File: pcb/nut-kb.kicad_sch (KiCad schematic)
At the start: 24 parts, among them SW1 SW_Push, U1 ATmega32U4-A, Y1 16 MHz

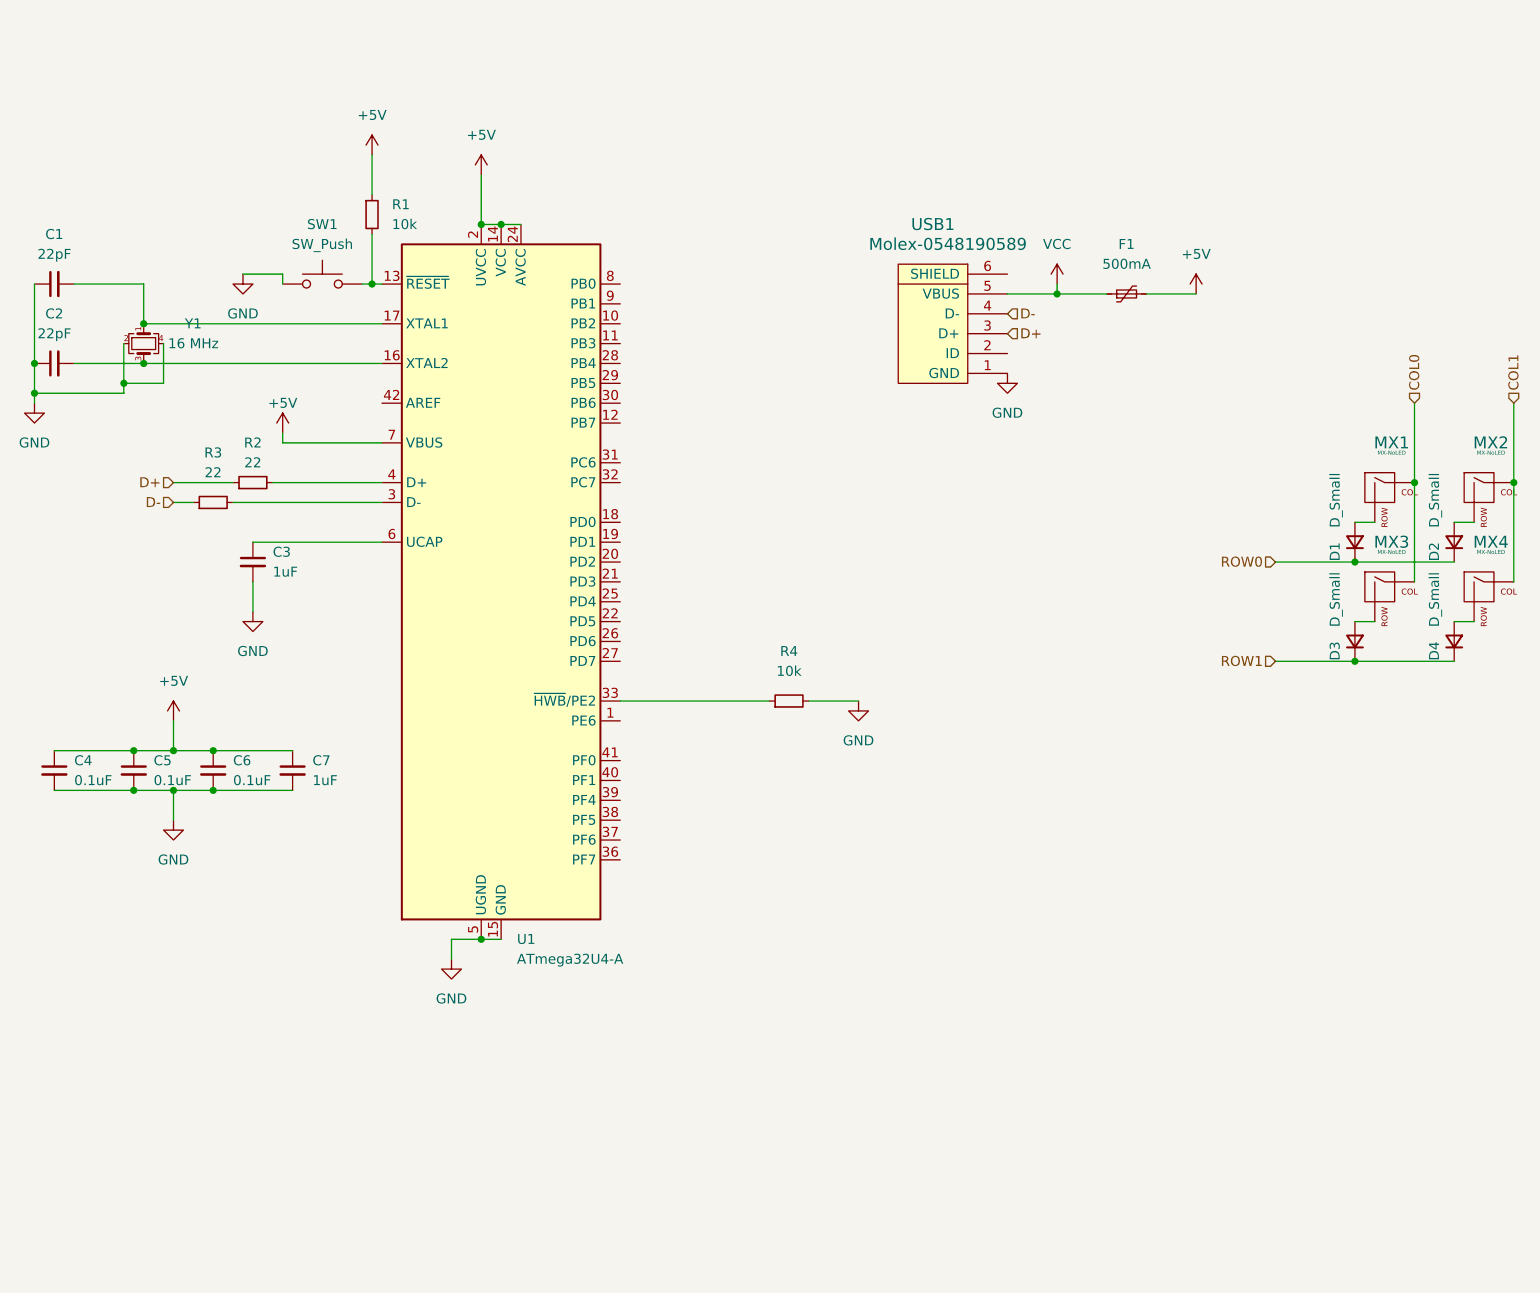
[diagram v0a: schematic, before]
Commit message: [pcb] finish everything for MX
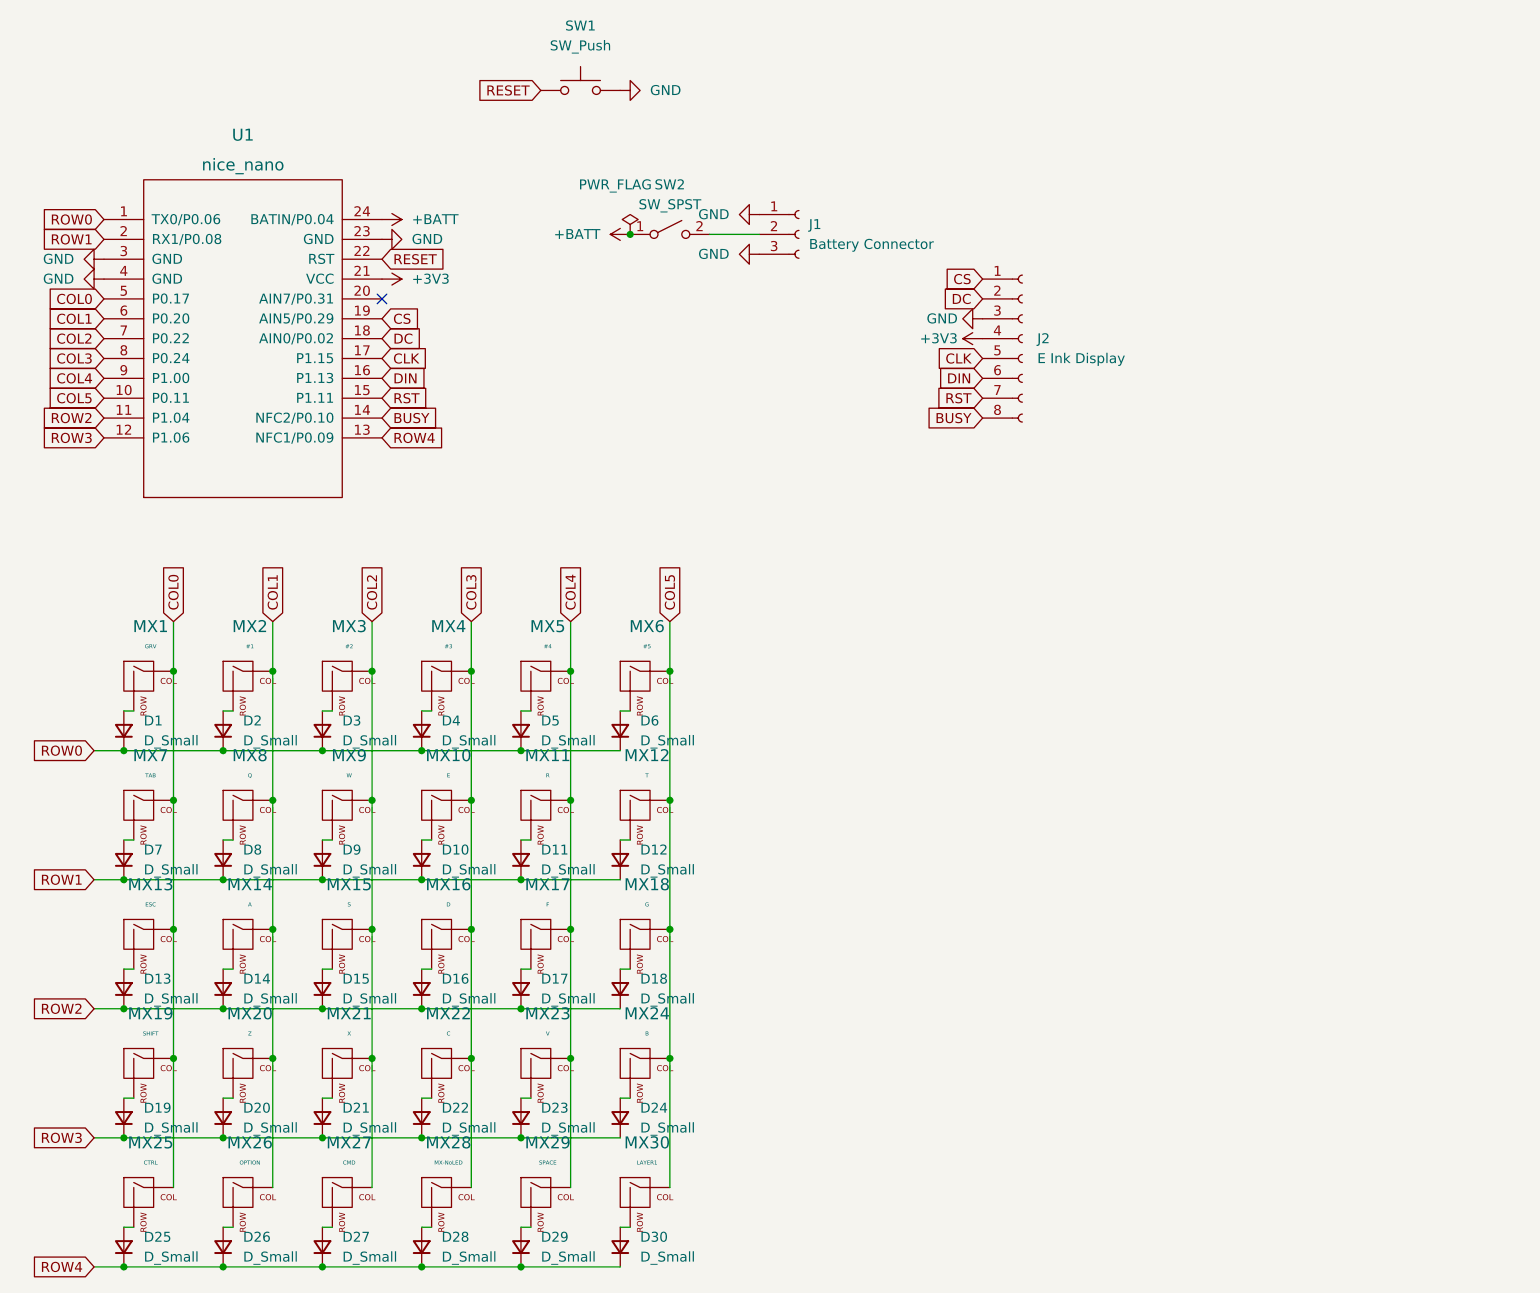
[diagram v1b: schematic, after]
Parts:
- removed C1, C2: 22pF, Capacitor_SMD:C_0805_2012Metric, symbol Device:C_Small
- removed C3, C7: 1uF, Capacitor_SMD:C_0805_2012Metric, symbol Device:C_Small
- removed C4, C5, C6: 0.1uF, Capacitor_SMD:C_0805_2012Metric, symbol Device:C_Small
- removed F1: 500mA, Fuse:Fuse_1206_3216Metric, symbol Device:Polyfuse_Small
- removed R1, R4: 10k, Resistor_SMD:R_0805_2012Metric, symbol Device:R_Small
- removed R2, R3: 22, Resistor_SMD:R_0805_2012Metric, symbol Device:R_Small
- removed U1: ATmega32U4-A, Package_QFP:TQFP-44_10x10mm_P0.8mm, symbol MCU_Microchip_ATmega:ATmega32U4-A
- removed USB1: Molex-0548190589, random-keyboard-parts:Molex-0548190589, symbol random-keyboard-parts:Molex-0548190589
- removed Y1: 16 MHz, Package_QFP:TQFP-44_10x10mm_P0.8mm, symbol Device:Crystal_GND24_Small
- added D10, D11, D12, D13, D14, D15, D16, D17, D18, D19, D20, D21, D22, D23, D24, D25, D26, D27, D28, D29, D30, D5, D6, D7, D8, D9: D_Small, Diode_SMD:D_SOD-123, symbol Device:D_Small
- added J1: Battery Connector, Connector_JST:JST_PH_B3B-PH-K_1x03_P2.00mm_Vertical, symbol Connector:Conn_01x03_Female
- added J2: E Ink Display, Connector_PinSocket_2.54mm:PinSocket_1x08_P2.54mm_Vertical, symbol Connector:Conn_01x08_Female
- added MX10: E, MX_Only:MXOnly-1U-Hotswap-Antishear, symbol MX_Alps_Hybrid:MX-NoLED
- added MX11: R, MX_Only:MXOnly-1U-Hotswap-Antishear, symbol MX_Alps_Hybrid:MX-NoLED
- added MX12: T, MX_Only:MXOnly-1U-Hotswap-Antishear, symbol MX_Alps_Hybrid:MX-NoLED
- added MX13: ESC, MX_Only:MXOnly-1U-Hotswap-Antishear, symbol MX_Alps_Hybrid:MX-NoLED
- added MX14: A, MX_Only:MXOnly-1U-Hotswap-Antishear, symbol MX_Alps_Hybrid:MX-NoLED
- added MX15: S, MX_Only:MXOnly-1U-Hotswap-Antishear, symbol MX_Alps_Hybrid:MX-NoLED
- added MX16: D, MX_Only:MXOnly-1U-Hotswap-Antishear, symbol MX_Alps_Hybrid:MX-NoLED
- added MX17: F, MX_Only:MXOnly-1U-Hotswap-Antishear, symbol MX_Alps_Hybrid:MX-NoLED
- added MX18: G, MX_Only:MXOnly-1U-Hotswap-Antishear, symbol MX_Alps_Hybrid:MX-NoLED
- added MX19: SHIFT, MX_Only:MXOnly-1U-Hotswap-Antishear, symbol MX_Alps_Hybrid:MX-NoLED
- added MX20: Z, MX_Only:MXOnly-1U-Hotswap-Antishear, symbol MX_Alps_Hybrid:MX-NoLED
- added MX21: X, MX_Only:MXOnly-1U-Hotswap-Antishear, symbol MX_Alps_Hybrid:MX-NoLED
- added MX22: C, MX_Only:MXOnly-1U-Hotswap-Antishear, symbol MX_Alps_Hybrid:MX-NoLED
- added MX23: V, MX_Only:MXOnly-1U-Hotswap-Antishear, symbol MX_Alps_Hybrid:MX-NoLED
- added MX24: B, MX_Only:MXOnly-1U-Hotswap-Antishear, symbol MX_Alps_Hybrid:MX-NoLED
- added MX25: CTRL, MX_Only:MXOnly-1U-Hotswap-Antishear, symbol MX_Alps_Hybrid:MX-NoLED
- added MX26: OPTION, MX_Only:MXOnly-1U-Hotswap-Antishear, symbol MX_Alps_Hybrid:MX-NoLED
- added MX27: CMD, MX_Only:MXOnly-1U-Hotswap-Antishear, symbol MX_Alps_Hybrid:MX-NoLED
- added MX28: MX-NoLED, MX_Only:MXOnly-1U-Hotswap-Antishear, symbol MX_Alps_Hybrid:MX-NoLED
- added MX29: SPACE, MX_Only:MXOnly-2U-Hotswap, symbol MX_Alps_Hybrid:MX-NoLED
- added MX30: LAYER1, MX_Only:MXOnly-2U-Hotswap, symbol MX_Alps_Hybrid:MX-NoLED
- added MX5: #4, MX_Only:MXOnly-1U-Hotswap-Antishear, symbol MX_Alps_Hybrid:MX-NoLED
- added MX6: #5, MX_Only:MXOnly-1U-Hotswap-Antishear, symbol MX_Alps_Hybrid:MX-NoLED
- added MX7: TAB, MX_Only:MXOnly-1U-Hotswap-Antishear, symbol MX_Alps_Hybrid:MX-NoLED
- added MX8: Q, MX_Only:MXOnly-1U-Hotswap-Antishear, symbol MX_Alps_Hybrid:MX-NoLED
- added MX9: W, MX_Only:MXOnly-1U-Hotswap-Antishear, symbol MX_Alps_Hybrid:MX-NoLED
- added SW2: SW_SPST, Button_Switch_THT:SW_DIP_SPSTx01_Slide_6.7x4.1mm_W7.62mm_P2.54mm_LowProfile, symbol Switch:SW_SPST
- added U1: nice_nano, nice-nano-kicad:nice_nano, symbol nice_nano:nice_nano
- MX1: value MX-NoLED -> GRV; footprint MX_Alps_Hybrid:MX-1U-NoLED -> MX_Only:MXOnly-1U-Hotswap-Antishear
- MX2: value MX-NoLED -> #1; footprint MX_Alps_Hybrid:MX-1U-NoLED -> MX_Only:MXOnly-1U-Hotswap-Antishear
- MX3: value MX-NoLED -> #2; footprint MX_Alps_Hybrid:MX-1U-NoLED -> MX_Only:MXOnly-1U-Hotswap-Antishear
- MX4: value MX-NoLED -> #3; footprint MX_Alps_Hybrid:MX-1U-NoLED -> MX_Only:MXOnly-1U-Hotswap-Antishear
- SW1: footprint random-keyboard-parts:SKQG-1155865 -> Button_Switch_THT:SW_DIP_SPSTx01_Slide_6.7x4.1mm_W7.62mm_P2.54mm_LowProfile
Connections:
- net COL0: now also MX13.1 (COL), MX19.1 (COL), MX25.1 (COL), MX7.1 (COL), U1.5 (P0.17); no longer MX3.1 (COL)
- net COL1: now also MX14.1 (COL), MX20.1 (COL), MX26.1 (COL), MX8.1 (COL), U1.6 (P0.20); no longer MX4.1 (COL)
- net GND: now also SW1.2, J1.1 (Pin_1), J1.3 (Pin_3), J2.3 (Pin_3), U1.23 (GND), U1.3 (GND), U1.4 (GND); no longer SW1.1
- net ROW0: now also D3.1 (K), D4.1 (K), D5.1 (K), D6.1 (K), U1.1 (TX0/P0.06)
- net ROW1: now also D10.1 (K), D11.1 (K), D12.1 (K), D7.1 (K), D8.1 (K), D9.1 (K), U1.2 (RX1/P0.08); no longer D3.1 (K), D4.1 (K)
- new net: D19.2 (A), MX19.2 (ROW)
- new net: D20.2 (A), MX20.2 (ROW)
- new net: D26.2 (A), MX26.2 (ROW)
- new net: D21.2 (A), MX21.2 (ROW)
- new net: D29.2 (A), MX29.2 (ROW)
- new net: D24.2 (A), MX24.2 (ROW)
- new net: D17.2 (A), MX17.2 (ROW)
- new net: D12.2 (A), MX12.2 (ROW)
- new net: D7.2 (A), MX7.2 (ROW)
- new net: D22.2 (A), MX22.2 (ROW)
- new net: D30.2 (A), MX30.2 (ROW)
- new net: D6.2 (A), MX6.2 (ROW)
- new net: J1.2 (Pin_2), SW2.2 (B)
- new net: D15.2 (A), MX15.2 (ROW)
- new net: D18.2 (A), MX18.2 (ROW)
- new net: D16.2 (A), MX16.2 (ROW)
- new net: D23.2 (A), MX23.2 (ROW)
- new net: D13.2 (A), MX13.2 (ROW)
- new net: D28.2 (A), MX28.2 (ROW)
- new net: D14.2 (A), MX14.2 (ROW)
- new net: D27.2 (A), MX27.2 (ROW)
- new net: D25.2 (A), MX25.2 (ROW)
- new net: D9.2 (A), MX9.2 (ROW)
- new net: D11.2 (A), MX11.2 (ROW)
- new net: D8.2 (A), MX8.2 (ROW)
- new net: D10.2 (A), MX10.2 (ROW)
- new net: D5.2 (A), MX5.2 (ROW)
- new net +3V3: J2.4 (Pin_4), U1.21 (VCC)
- new net +BATT: SW2.1 (A), U1.24 (BATIN/P0.04)
- new net BUSY: J2.8 (Pin_8), U1.14 (NFC2/P0.10)
- new net CLK: J2.5 (Pin_5), U1.17 (P1.15)
- new net COL2: MX15.1 (COL), MX21.1 (COL), MX27.1 (COL), MX3.1 (COL), MX9.1 (COL), U1.7 (P0.22)
- new net COL3: MX10.1 (COL), MX16.1 (COL), MX22.1 (COL), MX28.1 (COL), MX4.1 (COL), U1.8 (P0.24)
- new net COL4: MX11.1 (COL), MX17.1 (COL), MX23.1 (COL), MX29.1 (COL), MX5.1 (COL), U1.9 (P1.00)
- new net COL5: MX12.1 (COL), MX18.1 (COL), MX24.1 (COL), MX30.1 (COL), MX6.1 (COL), U1.10 (P0.11)
- new net CS: J2.1 (asdf), U1.19 (AIN5/P0.29)
- new net DC: J2.2 (Pin_2), U1.18 (AIN0/P0.02)
- new net DIN: J2.6 (Pin_6), U1.16 (P1.13)
- new net RESET: SW1.1, U1.22 (RST)
- new net ROW2: D13.1 (K), D14.1 (K), D15.1 (K), D16.1 (K), D17.1 (K), D18.1 (K), U1.11 (P1.04)
- new net ROW3: D19.1 (K), D20.1 (K), D21.1 (K), D22.1 (K), D23.1 (K), D24.1 (K), U1.12 (P1.06)
- new net ROW4: D25.1 (K), D26.1 (K), D27.1 (K), D28.1 (K), D29.1 (K), D30.1 (K), U1.13 (NFC1/P0.09)
- new net RST: J2.7 (Pin_7), U1.15 (P1.11)
- no-connect marks 0 -> 1
